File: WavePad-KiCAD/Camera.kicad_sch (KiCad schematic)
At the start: 20 parts, among them J4 Conn_02x15_Counter_Clockwise, U1 ESP32-S3-MINI-1U, U10 MIC5504-2.8YM5, U11 MIC5504-1.2YM5, U12 SN74LVC8T245 - OUT, U15 TXS0102DCU, U17 SN74LVC8T245 - IN, U2 MIC5504-1.8YM5, U3 SN74LVC8T245 - OUT

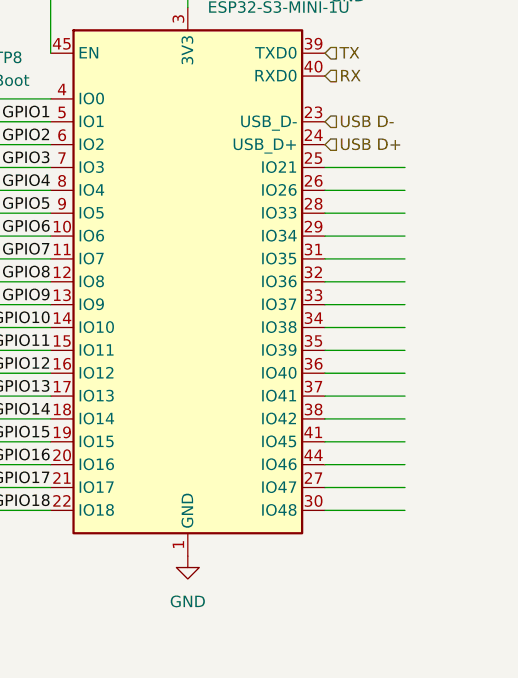
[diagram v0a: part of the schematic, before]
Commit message: Started PCB
Added CSI and DSI connector as well as a USB C with protected  data and Power
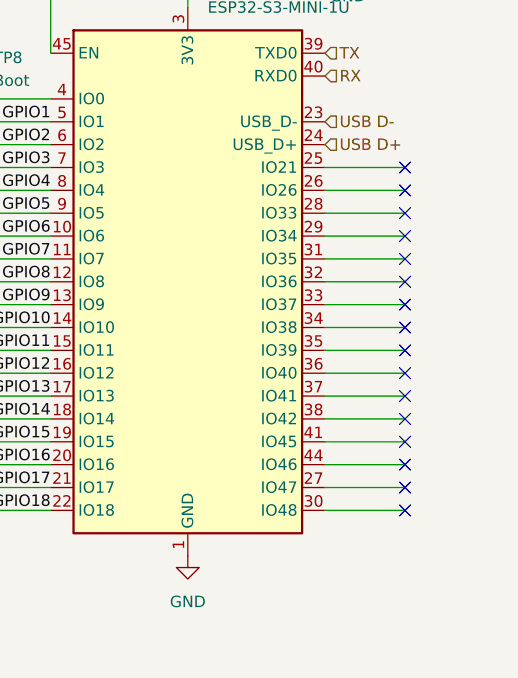
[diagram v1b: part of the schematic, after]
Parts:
- R21, R22: footprint (none) -> Resistor_SMD:R_0402_1005Metric
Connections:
- no-connect marks 3 -> 19
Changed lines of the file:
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@@
 (kicad_sch
-	(version 20231120)
+	(version 20250114)
 	(generator "eeschema")
-	(generator_version "8.0")
+	(generator_version "9.0")
 	(paper "A4")
 	(title_block
@@
 	)
 	(no_connect
+		(at 278.13 114.3)
+	)
+	(no_connect
+		(at 278.13 86.36)
+	)
+	(no_connect
+		(at 278.13 109.22)
+	)
+	(no_connect
+		(at 278.13 93.98)
+	)
+	(no_connect
 		(at 19.05 125.73)
 	)
 	(no_connect
+		(at 278.13 78.74)
+	)
+	(no_connect
+		(at 278.13 83.82)
+	)
+	(no_connect
+		(at 278.13 76.2)
+	)
+	(no_connect
+		(at 278.13 106.68)
+	)
+	(no_connect
+		(at 278.13 104.14)
+	)
+	(no_connect
 		(at 19.05 95.25)
 	)
 	(no_connect
+		(at 278.13 81.28)
+	)
+	(no_connect
+		(at 278.13 99.06)
+	)
+	(no_connect
+		(at 278.13 101.6)
+	)
+	(no_connect
+		(at 278.13 91.44)
+	)
+	(no_connect
+		(at 278.13 88.9)
+	)
+	(no_connect
 		(at 19.05 92.71)
 	)
+	(no_connect
+		(at 278.13 111.76)
+	)
+	(no_connect
+		(at 278.13 96.52)
+	)
 	(wire
 		(pts
@@
 			)
 		)
-		(property "Footprint" ""
+		(property "Footprint" "Resistor_SMD:R_0402_1005Metric"
 			(at 189.23 105.41 0)
 			(effects
@@
 			)
 		)
-		(property "Footprint" ""
+		(property "Footprint" "Resistor_SMD:R_0402_1005Metric"
 			(at 189.23 120.65 0)
 			(effects
